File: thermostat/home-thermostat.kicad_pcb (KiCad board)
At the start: 4 copper layers, 98.6 x 50.2 mm, 133 parts, among them J1 Amphenol_132289 SMA, J2 Conn_01x24, J3 Thermosthat - Molex PicoBlade, J4 Conn_ARM_JTAG_SWD_10, J5 Conn_01x20, J6 Conn_02x02_Odd_Even, J7 UART, Q1 BSS806NL6327, Q2 BSS806NL6327, Q3 BSS806NL6327, Q4 BSS806NL6327, Q5 BSS806NL6327, Q6 BSS806NL6327, U1 MKW41Z512VHT, U10 SN74LVC2T45DCUR, U2 MCP7940N-xMS, U3 MCP9844, U4 AT24C512, U5 LM2574M-5, U6 LD1117S33TR_SOT223, U7 LM358, U8 PCF8574, U9 SN74LVC2T45DCUR, Y1 32MHz 10PPM SMT 2.0x1.6mm 10PF, Y2 32.768KHz 20PPM 3.2x1.5mm 7PF, Y3 32.768KHz 20PPM 3.2x1.5mm 7PF

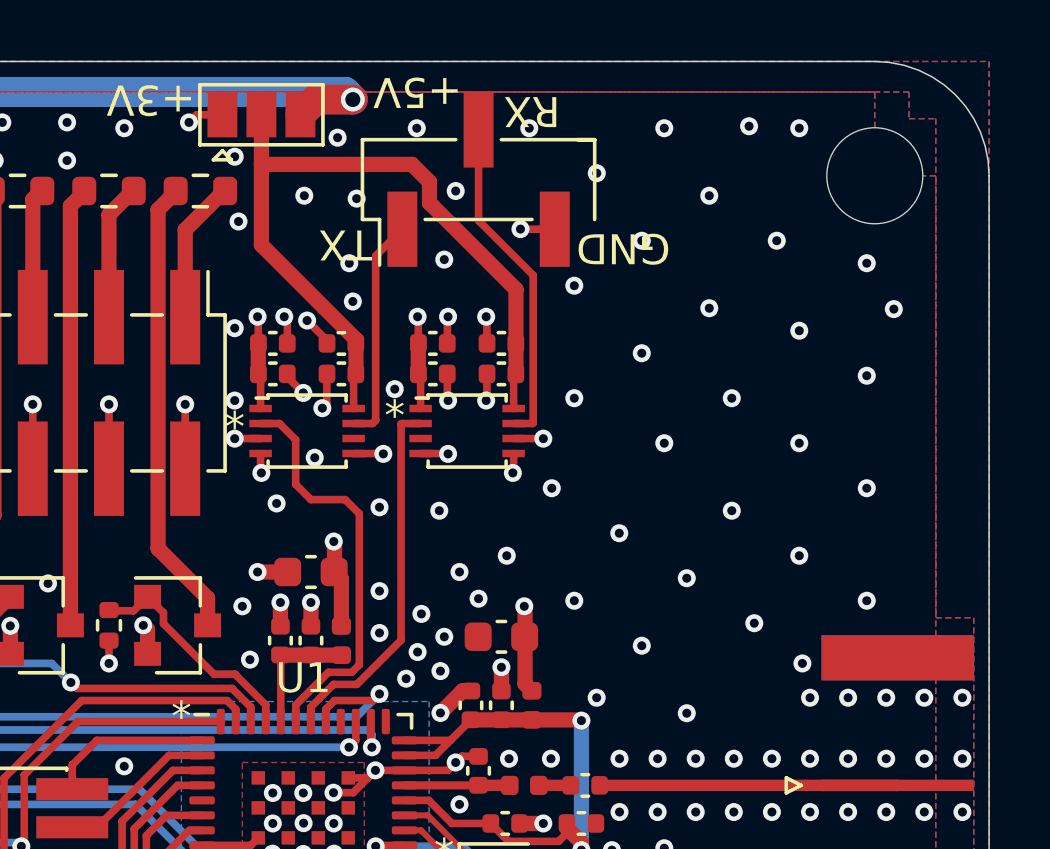
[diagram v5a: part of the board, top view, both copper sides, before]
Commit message: Changed UART level shifter package on thermosthat, however there is not enough space on tempsensor.
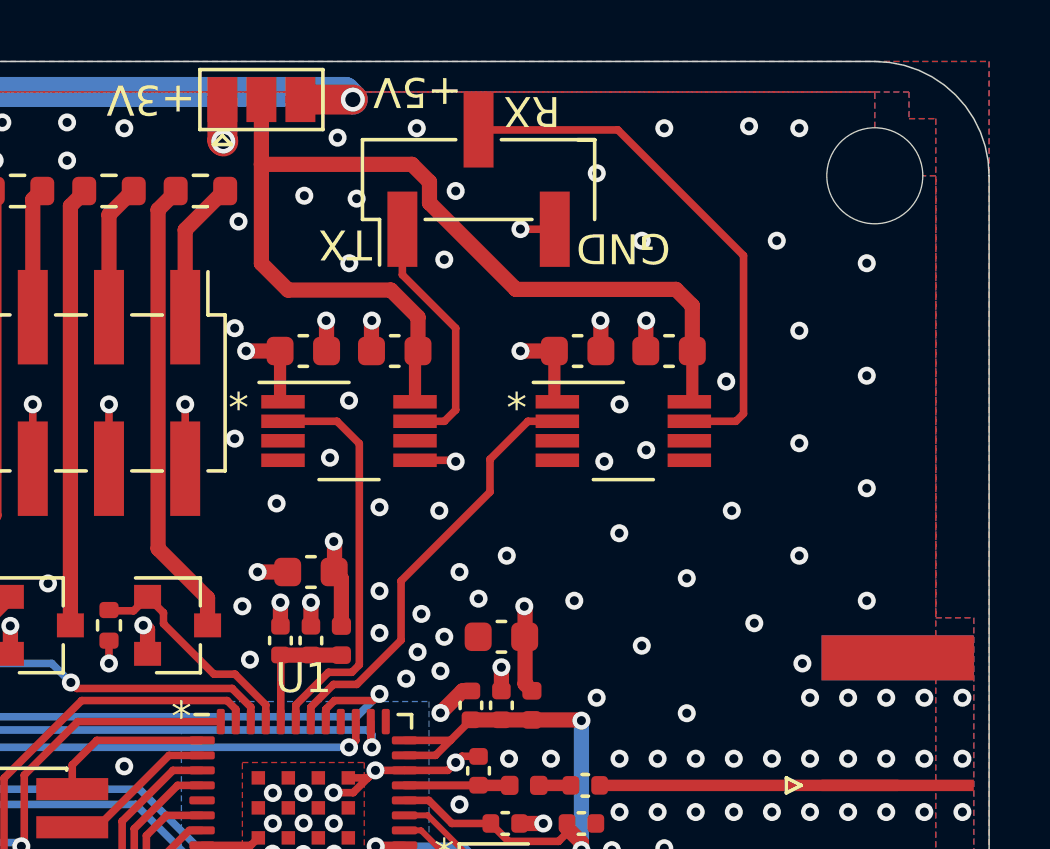
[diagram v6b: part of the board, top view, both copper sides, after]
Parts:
- removed C29, C48, C56, C59: 0,1u, Capacitor_SMD:C_0402_1005Metric
- C46, C47, C57, C58: value 1u -> 100n; footprint Capacitor_SMD:C_0402_1005Metric -> Capacitor_SMD:C_0603_1608Metric
- R23, R24, R25: value 0? -> 10K
- U10, U9: footprint Package_SO:VSSOP-8_2.4x2.1mm_P0.5mm -> Package_SO:VSSOP-8_3.0x3.0mm_P0.65mm
- moved C58 5.59 mm to (161.3, 83.7)
- moved U10 5.21 mm to (159.8, 86.4)
- moved C57 4.83 mm to (158.2, 83.7)
- moved C47 1.80 mm to (152.1, 83.7)
- moved U9 1.40 mm to (150.6, 86.4)
- moved C46 1.05 mm to (149.1, 83.7)
- moved JP1 0.51 mm to (147.7, 75.3)
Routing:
- net Net-(C47-Pad1): track 25.8 -> 34.3 mm
- net GND: track 120.8 -> 113.2 mm, vias 498 -> 481
- net /UART_RX: track 11.2 -> 17.7 mm
- net /LPUART0_RX: track 12.3 -> 14.4 mm
- net /UART_TX: track 7.52 -> 8.27 mm
